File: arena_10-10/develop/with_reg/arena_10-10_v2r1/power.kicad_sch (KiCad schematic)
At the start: 6 parts, among them J25 Barrel_Jack, J26 XT30 Female, SW1 SW_SPDT, U110 NID100-5, U82 RB-XXYYD

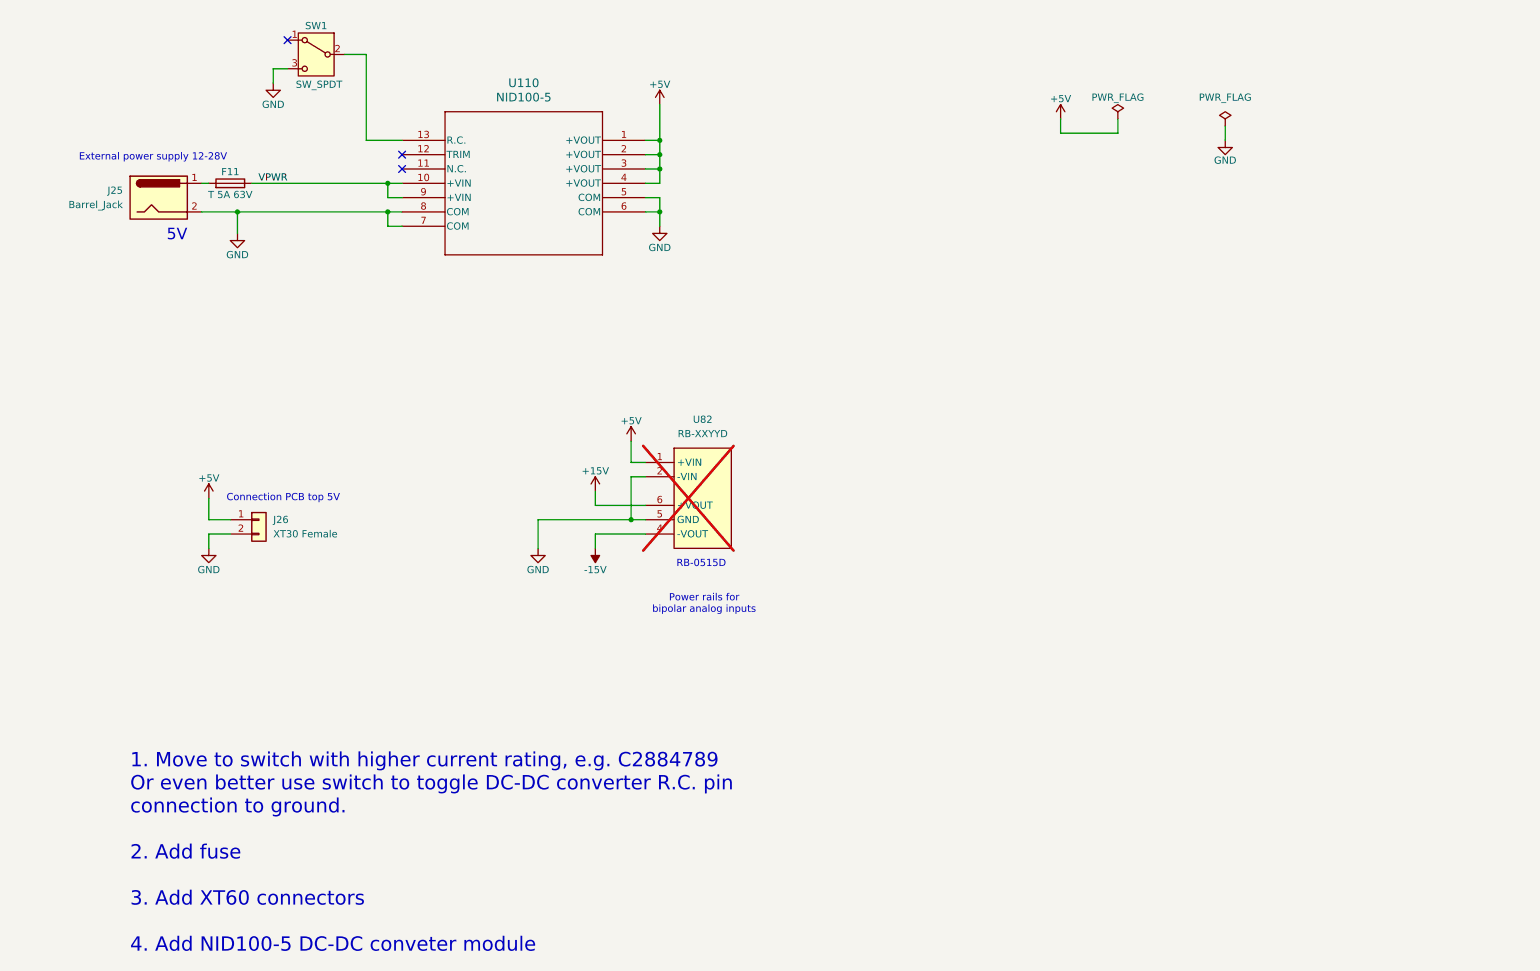
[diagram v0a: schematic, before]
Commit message: Modified notes, moved XT30 connectors.
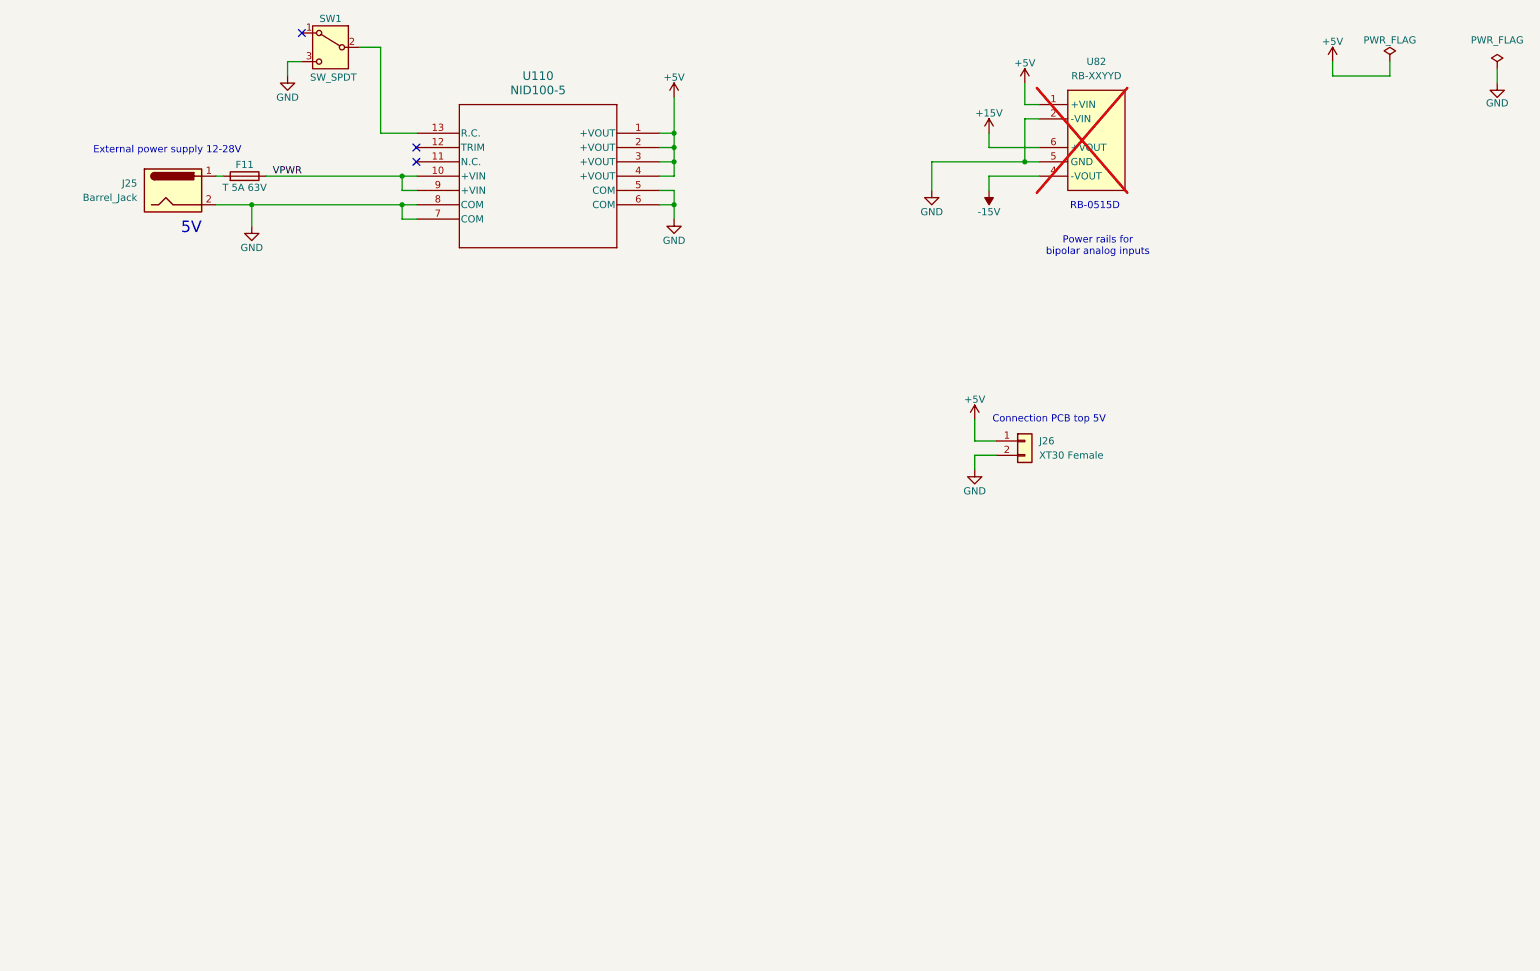
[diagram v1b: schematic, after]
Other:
- note removed: "1. Move to switch with higher current rating, e.g. C2884789 Or even better use switch to toggle DC-DC converter R.C. pin connection to ground. 2. Add fuse 3. Add XT60 connectors 4. Add NID100-5 DC-DC conveter module"
- moved on the sheet: F11, J25, J26, SW1, U110, U82

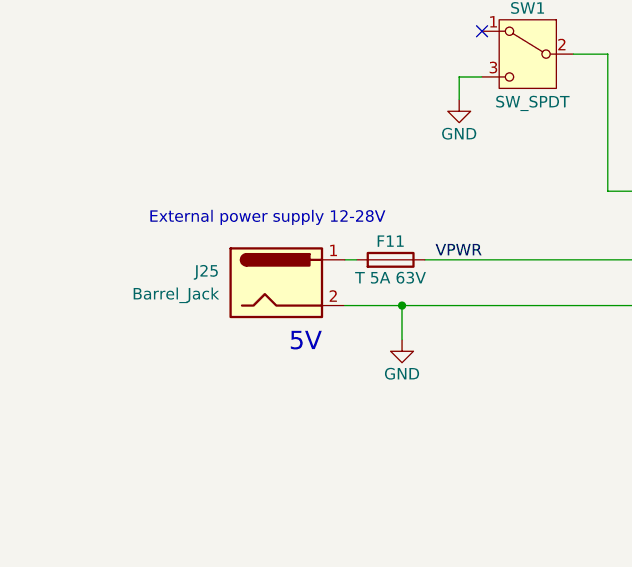
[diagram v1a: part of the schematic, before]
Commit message: Added zones around NID100-5 and jack.
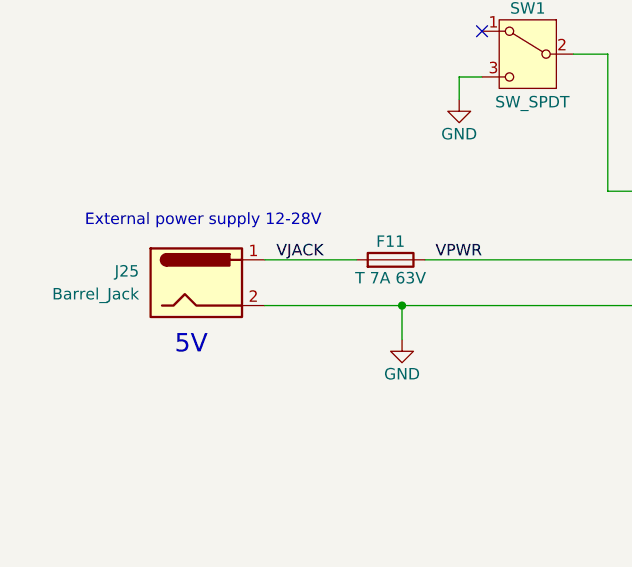
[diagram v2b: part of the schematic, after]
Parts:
- F11: value T 5A 63V -> T 7A 63V; LCSC Part # C1972666 -> C1972821
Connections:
- net VJACK: now reaches F11.2, J25.1
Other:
- moved on the sheet: J25
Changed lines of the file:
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@@
 	(text "External power supply 12-28V"
 		(exclude_from_sim no)
-		(at 38.354 44.958 0)
+		(at 31.242 45.212 0)
 		(effects
 			(font
@@
 	(text "5V"
 		(exclude_from_sim no)
-		(at 44.45 59.944 0)
+		(at 31.75 60.198 0)
 		(effects
 			(font
@@
 	(wire
 		(pts
-			(xy 53.34 54.61) (xy 46.99 54.61)
+			(xy 53.34 54.61) (xy 38.1 54.61)
 		)
 		(stroke
@@
 	(wire
 		(pts
-			(xy 48.26 49.53) (xy 46.99 49.53)
+			(xy 48.26 49.53) (xy 38.1 49.53)
 		)
 		(stroke
@@
 			)
 			(justify right bottom)
+		)
+	)
+	(label "VJACK"
+		(at 39.37 49.53 0)
+		(effects
+			(font
+				(size 1.27 1.27)
+			)
+			(justify left bottom)
 		)
 	)
@@
 			)
 		)
-		(property "Value" "T 5A 63V"
+		(property "Value" "T 7A 63V"
 			(at 52.07 51.562 90)
 			(show_name no)
@@
 			)
 		)
-		(property "LCSC Part #" "C1972666"
+		(property "LCSC Part #" "C1972821"
 			(at 52.07 49.53 90)
 			(hide yes)
@@
 	(symbol
 		(lib_id "Connector:Barrel_Jack")
-		(at 39.37 52.07 0)
+		(at 30.48 52.07 0)
 		(unit 1)
 		(body_style 1)
@@
 		(fields_autoplaced yes)
 		(property "Reference" "J25"
-			(at 33.02 50.7999 0)
+			(at 24.13 50.7999 0)
 			(show_name no)
 			(do_not_autoplace no)
@@
 		)
 		(property "Value" "Barrel_Jack"
-			(at 33.02 53.3399 0)
+			(at 24.13 53.3399 0)
 			(show_name no)
 			(do_not_autoplace no)
@@
 		)
 		(property "Footprint" "arena_custom:DC-053D-20A"
-			(at 40.64 53.086 0)
+			(at 31.75 53.086 0)
 			(hide yes)
 			(show_name no)
@@
 		)
 		(property "Datasheet" ""
-			(at 40.64 53.086 0)
+			(at 31.75 53.086 0)
 			(hide yes)
 			(show_name no)
@@
 		)
 		(property "Description" "DC Barrel Jack"
-			(at 39.37 52.07 0)
+			(at 30.48 52.07 0)
 			(hide yes)
 			(show_name no)
@@
 		)
 		(property "LCSC Part #" "C707274"
-			(at 39.37 52.07 0)
+			(at 30.48 52.07 0)
 			(hide yes)
 			(show_name no)
@@
 		)
 		(property "FT Position Offset" "0,-1.143"
-			(at 39.37 52.07 0)
-			(hide yes)
-			(show_name no)
+			(at 30.48 52.07 0)
+			(hide yes)
+			(show_name no)
